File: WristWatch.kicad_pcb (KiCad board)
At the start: 4 copper layers, 59.9 x 59.9 mm, 144 parts

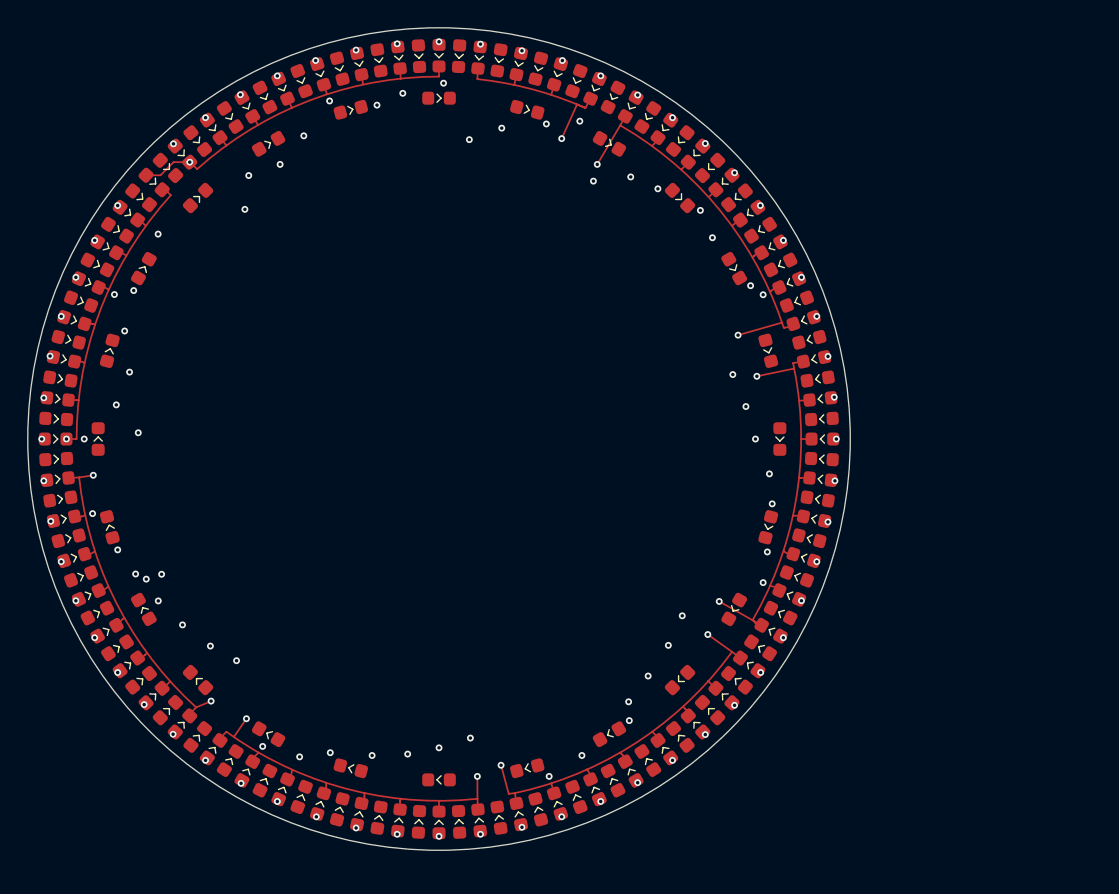
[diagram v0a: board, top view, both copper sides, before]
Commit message: Unknown progress. Pending twisted charlieplex experiments
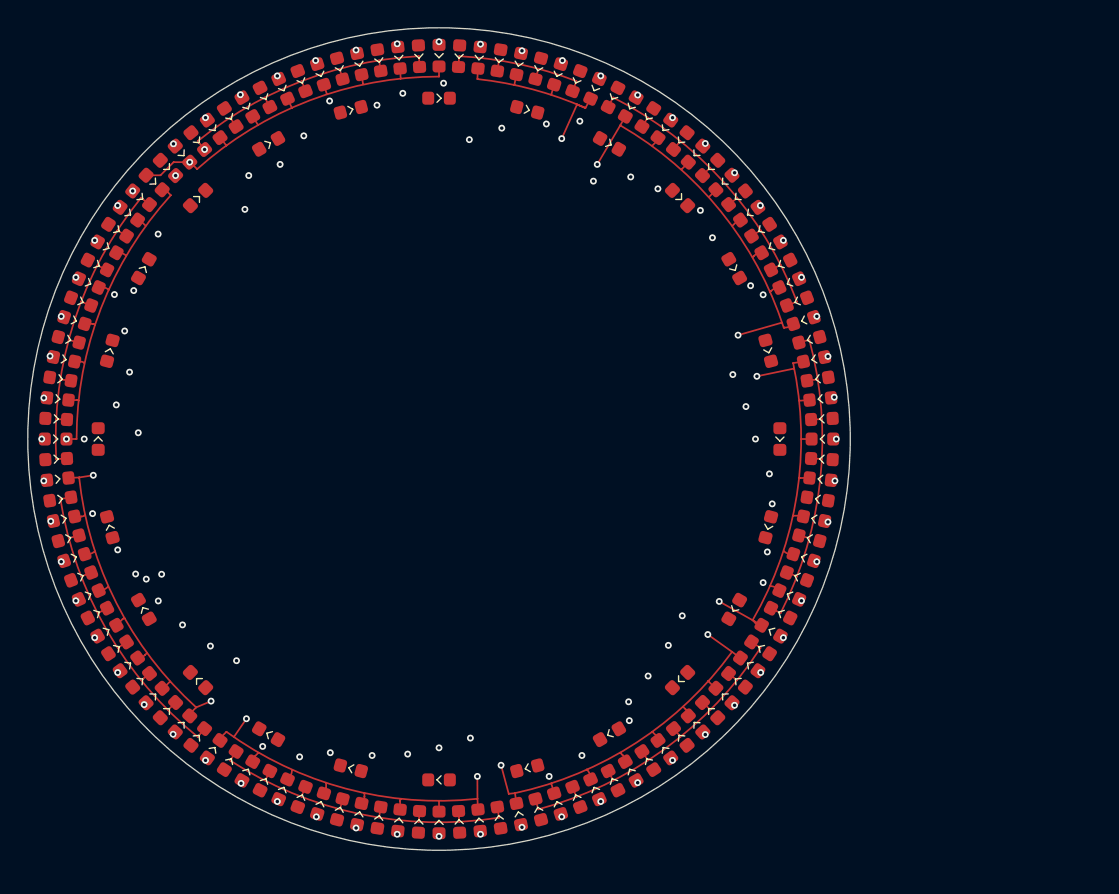
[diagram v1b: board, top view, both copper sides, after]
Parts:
- removed the D121 at (-6.43, -24.0)
- added D144: LED_Small, LED_SMD:LED_0603_1608Metric, F.Cu at (6.43, -24.0)
- D100, D101, D102, D103, D104, D105, D106, D107, D108, D109, D110, D111, D112, D113, D114, D115, D116, D117, D118, D119, D120, D61, D62, D63, D64, D65, D66, D67, D68, D69, D70, D71, D72, D73, D74, D75, D76, D77, D78, D79, D80, D81, D82, D83, D84, D85, D86, D87, D88, D89, D90, D91, D92, D93, D94, D95, D96, D97, D98, D99: value LED_0603_1608Metric -> LED_Small
- moved D126 6.48 mm to (-24.0, -6.43), turned to -105 degrees
- moved D127 6.48 mm to (-24.8, 0.00), turned to -90 degrees
- moved D132 6.48 mm to (-6.43, 24.0), turned to -15 degrees
- moved D133 6.48 mm to (0.00, 24.8), turned to 0 degrees
- moved D138 6.48 mm to (24.0, 6.43), turned to 75 degrees
- moved D139 6.48 mm to (24.8, 0.00), turned to 90 degrees
- moved D122 6.48 mm to (-6.43, -24.0), turned to -165 degrees
- moved D125 6.48 mm to (-21.5, -12.4), turned to -120 degrees
- moved D128 6.48 mm to (-24.0, 6.43), turned to -75 degrees
- moved D131 6.48 mm to (-12.4, 21.5), turned to -30 degrees
- moved D134 6.48 mm to (6.43, 24.0), turned to 15 degrees
- moved D137 6.48 mm to (21.5, 12.4), turned to 60 degrees
- moved D140 6.48 mm to (24.0, -6.43), turned to 105 degrees
- moved D143 6.48 mm to (12.4, -21.5), turned to 150 degrees
- moved D123 6.48 mm to (-12.4, -21.5), turned to -150 degrees
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- renumbered D1 to D121
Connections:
- D100 pad 1: (no net) -> CB5
- D100 pad 2: (no net) -> CB9
- D101 pad 1: (no net) -> CB6
- D101 pad 2: (no net) -> CB1
- D102 pad 1: (no net) -> CB6
- D102 pad 2: (no net) -> CB2
- D103 pad 1: (no net) -> CB6
- D103 pad 2: (no net) -> CB3
- D104 pad 1: (no net) -> CB6
- D104 pad 2: (no net) -> CB4
- D105 pad 1: (no net) -> CB6
- D105 pad 2: (no net) -> CB5
- D106 pad 1: (no net) -> CB6
- D106 pad 2: (no net) -> CB7
- D107 pad 1: (no net) -> CB6
- D107 pad 2: (no net) -> CB8
- D108 pad 1: (no net) -> CB6
- D108 pad 2: (no net) -> CB9
- D109 pad 1: (no net) -> CB7
- D109 pad 2: (no net) -> CB1
- D110 pad 1: (no net) -> CB7
- D110 pad 2: (no net) -> CB2
- D111 pad 1: (no net) -> CB7
- D111 pad 2: (no net) -> CB3
- D112 pad 1: (no net) -> CB7
- D112 pad 2: (no net) -> CB4
- D113 pad 1: (no net) -> CB7
- D113 pad 2: (no net) -> CB5
- D114 pad 1: (no net) -> CB7
- D114 pad 2: (no net) -> CB6
- D115 pad 1: (no net) -> CB7
- D115 pad 2: (no net) -> CB8
- D116 pad 1: (no net) -> CB7
- D116 pad 2: (no net) -> CB9
- D117 pad 1: (no net) -> CB8
- D117 pad 2: (no net) -> CB5
- D118 pad 1: (no net) -> CB8
- D118 pad 2: (no net) -> CB6
- D119 pad 1: (no net) -> CB8
- D119 pad 2: (no net) -> CB7
- D120 pad 1: (no net) -> CB8
- D120 pad 2: (no net) -> CB9
- D121 pad 1: (no net) -> CC1
- D121 pad 2: (no net) -> CC2
- D122 pad 1: (no net) -> CC1
- D122 pad 2: (no net) -> CC3
- D123 pad 1: (no net) -> CC1
- D123 pad 2: (no net) -> CC4
- D124 pad 1: (no net) -> CC1
- D124 pad 2: (no net) -> CC5
- D125 pad 1: (no net) -> CC1
- D125 pad 2: (no net) -> CC6
- D126 pad 1: (no net) -> CC2
- D126 pad 2: (no net) -> CC1
- D127 pad 1: (no net) -> CC2
- D127 pad 2: (no net) -> CC3
- D128 pad 1: (no net) -> CC2
- D128 pad 2: (no net) -> CC4
- D129 pad 1: (no net) -> CC2
- D129 pad 2: (no net) -> CC5
- D130 pad 1: (no net) -> CC2
- D130 pad 2: (no net) -> CC6
- D131 pad 1: (no net) -> CC3
- D131 pad 2: (no net) -> CC1
- D132 pad 1: (no net) -> CC3
- D132 pad 2: (no net) -> CC2
- D133 pad 1: (no net) -> CC3
- D133 pad 2: (no net) -> CC4
- D134 pad 1: (no net) -> CC3
- D134 pad 2: (no net) -> CC5
- D135 pad 1: (no net) -> CC3
- D135 pad 2: (no net) -> CC6
- D136 pad 1: (no net) -> CC4
- D136 pad 2: (no net) -> CC1
- D137 pad 1: (no net) -> CC4
- D137 pad 2: (no net) -> CC2
- D138 pad 1: (no net) -> CC4
- D138 pad 2: (no net) -> CC3
- D139 pad 1: (no net) -> CC4
- D139 pad 2: (no net) -> CC5
- D140 pad 1: (no net) -> CC4
- D140 pad 2: (no net) -> CC6
- D141 pad 1: (no net) -> CC5
- D141 pad 2: (no net) -> CC1
- D142 pad 1: (no net) -> CC5
- D142 pad 2: (no net) -> CC2
- D143 pad 1: (no net) -> CC5
- D143 pad 2: (no net) -> CC3
- D61 pad 1: (no net) -> CB1
- D61 pad 2: (no net) -> CB2
- D62 pad 1: (no net) -> CB1
- D62 pad 2: (no net) -> CB3
- D63 pad 1: (no net) -> CB1
- D63 pad 2: (no net) -> CB4
- D64 pad 1: (no net) -> CB1
- D64 pad 2: (no net) -> CB5
- D65 pad 1: (no net) -> CB1
- D65 pad 2: (no net) -> CB6
- D66 pad 1: (no net) -> CB1
- D66 pad 2: (no net) -> CB7
- D67 pad 1: (no net) -> CB1
- D67 pad 2: (no net) -> CB8
- D68 pad 1: (no net) -> CB1
- D68 pad 2: (no net) -> CB9
- D69 pad 1: (no net) -> CB2
- D69 pad 2: (no net) -> CB1
- D70 pad 1: (no net) -> CB2
- D70 pad 2: (no net) -> CB3
- D71 pad 1: (no net) -> CB2
- D71 pad 2: (no net) -> CB4
- D72 pad 1: (no net) -> CB2
- D72 pad 2: (no net) -> CB5
- D73 pad 1: (no net) -> CB2
- D73 pad 2: (no net) -> CB6
- D74 pad 1: (no net) -> CB2
- D74 pad 2: (no net) -> CB7
- D75 pad 1: (no net) -> CB2
- D75 pad 2: (no net) -> CB8
- D76 pad 1: (no net) -> CB2
- D76 pad 2: (no net) -> CB9
- D77 pad 1: (no net) -> CB3
- D77 pad 2: (no net) -> CB1
- D78 pad 1: (no net) -> CB3
- D78 pad 2: (no net) -> CB2
- D79 pad 1: (no net) -> CB3
- D79 pad 2: (no net) -> CB4
- D80 pad 1: (no net) -> CB3
- D80 pad 2: (no net) -> CB5
- D81 pad 1: (no net) -> CB3
- D81 pad 2: (no net) -> CB6
- D82 pad 1: (no net) -> CB3
- D82 pad 2: (no net) -> CB7
- D83 pad 1: (no net) -> CB3
- D83 pad 2: (no net) -> CB8
- D84 pad 1: (no net) -> CB3
- D84 pad 2: (no net) -> CB9
- D85 pad 1: (no net) -> CB4
- D85 pad 2: (no net) -> CB1
- D86 pad 1: (no net) -> CB4
- D86 pad 2: (no net) -> CB2
- D87 pad 1: (no net) -> CB4
- D87 pad 2: (no net) -> CB3
- D88 pad 1: (no net) -> CB4
- D88 pad 2: (no net) -> CB5
- D89 pad 1: (no net) -> CB4
- D89 pad 2: (no net) -> CB6
- D90 pad 1: (no net) -> CB4
- D90 pad 2: (no net) -> CB7
- D91 pad 1: (no net) -> CB4
- D91 pad 2: (no net) -> CB8
- D92 pad 1: (no net) -> CB4
- D92 pad 2: (no net) -> CB9
- D93 pad 1: (no net) -> CB5
- D93 pad 2: (no net) -> CB1
- D94 pad 1: (no net) -> CB5
- D94 pad 2: (no net) -> CB2
- D95 pad 1: (no net) -> CB5
- D95 pad 2: (no net) -> CB3
- D96 pad 1: (no net) -> CB5
- D96 pad 2: (no net) -> CB4
- D97 pad 1: (no net) -> CB5
- D97 pad 2: (no net) -> CB6
- D98 pad 1: (no net) -> CB5
- D98 pad 2: (no net) -> CB7
- D99 pad 1: (no net) -> CB5
- D99 pad 2: (no net) -> CB8
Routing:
- net CB5: track 0.00 -> 6.31 mm
- net CB7: track 0.00 -> 6.27 mm
- net CB2: track 0.00 -> 6.24 mm
- net CB4: track 0.00 -> 6.23 mm
- net CB3: track 0.00 -> 6.16 mm
- net CB1: track 0.00 -> 5.51 mm, vias 0 -> 3
- net CB6: track 0.00 -> 5.45 mm
- net CB8: track 0.00 -> 3.13 mm

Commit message: Start layout. MCU close, LEDs correct, pending esp32
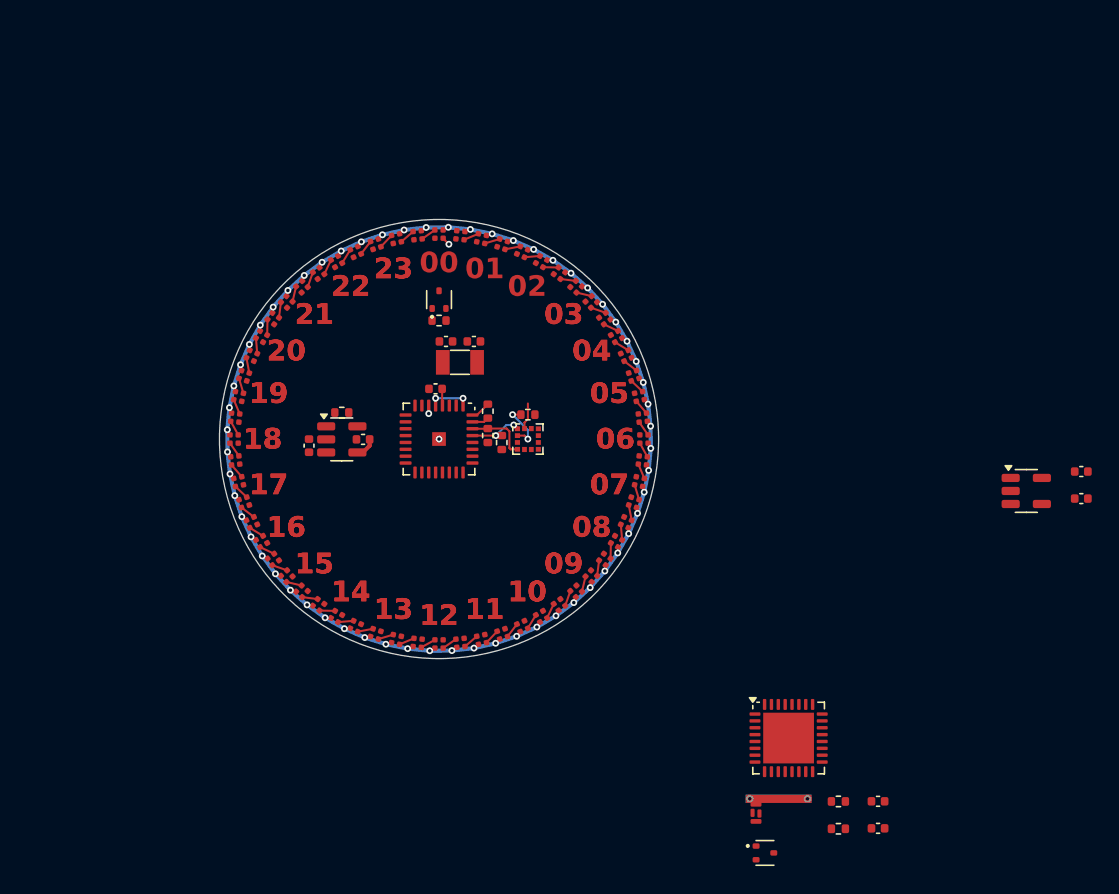
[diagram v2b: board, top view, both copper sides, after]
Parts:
- removed D100, D101, D102, D103, D104, D105, D106, D107, D108, D109, D110, D111, D112, D113, D114, D115, D116, D117, D118, D119, D120, D121, D122, D123, D124, D125, D126, D127, D128, D129, D130, D131, D132, D133, D134, D135, D136, D137, D138, D139, D140, D141, D142, D143, D144, D61, D62, D63, D64, D65, D66, D67, D68, D69, D70, D71, D72, D73, D74, D75, D76, D77, D78, D79, D80, D81, D82, D83, D84, D85, D86, D87, D88, D89, D90, D91, D92, D93, D94, D95, D96, D97, D98, D99: LED_Small, LED_SMD:LED_0603_1608Metric
- added AE1: Antenna_Shield, Antenna_SMD:C209892, F.Cu at (23.1, 27.8)
- added C1: 100n, Capacitor_SMD:C_0402_1005Metric, F.Cu at (-0.25, -3.66)
- added C12: 1u, Capacitor_SMD:C_0402_1005Metric, F.Cu at (46.8, 2.37)
- added C13: 2u2, Capacitor_SMD:C_0402_1005Metric, F.Cu at (46.8, 4.34)
- added C14: 4u7, Capacitor_SMD:C_0402_1005Metric, F.Cu at (-5.54, 0.03)
- added C15: 4u7, Capacitor_SMD:C_0402_1005Metric, F.Cu at (-9.47, 0.48)
- added C16: 12p, Capacitor_SMD:C_0402_1005Metric, F.Cu at (32.0, 26.4)
- added C17: 12p, Capacitor_SMD:C_0402_1005Metric, F.Cu at (32.0, 28.4)
- added C4: 4p3, Capacitor_SMD:C_0402_1005Metric, F.Cu at (2.54, -7.11)
- added C7: 4p3, Capacitor_SMD:C_0402_1005Metric, F.Cu at (0.51, -7.11)
- added Q1: Q_PMOS_GSD, Package_TO_SOT_SMD:SOT-523, F.Cu at (0.00, -10.2)
- added Q2: Q_PMOS_GSD, Package_TO_SOT_SMD:SOT-523, F.Cu at (23.8, 30.2)
- added R1: 10k, Resistor_SMD:R_0402_1005Metric, F.Cu at (3.56, -2.03)
- added R10: 10k, Resistor_SMD:R_0402_1005Metric, F.Cu at (-7.09, -1.93)
- added R11: 1M, Resistor_SMD:R_0402_1005Metric, F.Cu at (29.1, 26.4)
- added R12: 100k, Resistor_SMD:R_0402_1005Metric, F.Cu at (29.1, 28.4)
- added R6: 1M, Resistor_SMD:R_0402_1005Metric, F.Cu at (0.00, -8.64)
- added R7: 4k7, Resistor_SMD:R_0402_1005Metric, F.Cu at (4.57, 0.25)
- added R8: 4k7, Resistor_SMD:R_0402_1005Metric, F.Cu at (3.56, -0.25)
- added R9: 10k, Resistor_SMD:R_0402_1005Metric, F.Cu at (6.48, -1.78)
- added U2: STM32L412KBUx, Package_DFN_QFN:QFN-32-1EP_5x5mm_P0.5mm_EP3.45x3.45mm, F.Cu at (0.00, 0.00)
- added U3: LIS2DE12, Package_LGA:LGA-12_2x2mm_P0.5mm, F.Cu at (6.48, 0.00)
- added U4: AP2205-3.0, Package_TO_SOT_SMD:SOT-23-5, F.Cu at (42.8, 3.78)
- added U5: MCP73832-2-OT, Package_TO_SOT_SMD:SOT-23-5, F.Cu at (-7.09, 0.03)
- added U6: ESP32-C3, Package_DFN_QFN:QFN-32-1EP_5x5mm_P0.5mm_EP3.7x3.7mm, F.Cu at (25.5, 21.8)
- added Y1: 32.768k, Crystal:Crystal_SMD_3215-2Pin_3.2x1.5mm, F.Cu at (1.52, -5.59)
- D1, D10, D11, D12, D13, D14, D15, D16, D17, D18, D19, D2, D20, D21, D22, D23, D24, D25, D26, D27, D28, D29, D3, D30, D31, D32, D33, D34, D35, D36, D37, D38, D39, D4, D40, D41, D42, D43, D44, D45, D46, D47, D48, D49, D5, D50, D51, D52, D53, D54, D55, D56, D57, D58, D59, D6, D60, D7, D8, D9: value LED_Small -> WS2812B; footprint LED_SMD:LED_0603_1608Metric -> LED_Custom:XL-1010RGBC
- moved D15 13.0 mm to (-14.9, -1.56), turned to 84 degrees
- moved D17 13.0 mm to (-14.9, 1.56), turned to 96 degrees
- moved D2 13.0 mm to (-1.56, -14.9), turned to 6 degrees
- moved D30 13.0 mm to (-1.56, 14.9), turned to 174 degrees
- moved D32 13.0 mm to (1.56, 14.9), turned to -174 degrees
- moved D45 13.0 mm to (14.9, 1.56), turned to -96 degrees
- moved D47 13.0 mm to (14.9, -1.56), turned to -84 degrees
- moved D60 13.0 mm to (1.56, -14.9), turned to -6 degrees
- moved D12 13.0 mm to (-13.6, -6.07), turned to 66 degrees
- moved D20 13.0 mm to (-13.6, 6.07), turned to 114 degrees
- moved D27 13.0 mm to (-6.07, 13.6), turned to 156 degrees
- moved D35 13.0 mm to (6.07, 13.6), turned to -156 degrees
- moved D42 13.0 mm to (13.6, 6.07), turned to -114 degrees
- moved D5 13.0 mm to (-6.07, -13.6), turned to 24 degrees
- moved D50 13.0 mm to (13.6, -6.07), turned to -66 degrees
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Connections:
- D1 pad 1: CA1 -> VLED
- D1 pad 2: CA2 -> Net-(D1-DOUT)
- D10 pad 1: CA2 -> VLED
- D10 pad 2: CA3 -> Net-(D10-DOUT)
- D11 pad 1: CA2 -> VLED
- D11 pad 2: CA4 -> Net-(D11-DOUT)
- D12 pad 1: CA2 -> VLED
- D12 pad 2: CA5 -> Net-(D12-DOUT)
- D13 pad 1: CA2 -> VLED
- D13 pad 2: CA6 -> Net-(D13-DOUT)
- D14 pad 1: CA2 -> VLED
- D14 pad 2: CA7 -> Net-(D14-DOUT)
- D15 pad 1: CA2 -> VLED
- D15 pad 2: CA8 -> Bank1
- D16 pad 1: CA2 -> VLED
- D16 pad 2: CA9 -> Net-(D16-DOUT)
- D17 pad 1: CA3 -> VLED
- D17 pad 2: CA1 -> Net-(D17-DOUT)
- D18 pad 1: CA3 -> VLED
- D18 pad 2: CA2 -> Net-(D18-DOUT)
- D19 pad 1: CA3 -> VLED
- D19 pad 2: CA4 -> Net-(D19-DOUT)
- D2 pad 1: CA1 -> VLED
- D2 pad 2: CA3 -> Net-(D2-DOUT)
- D20 pad 1: CA3 -> VLED
- D20 pad 2: CA5 -> Net-(D20-DOUT)
- D21 pad 1: CA3 -> VLED
- D21 pad 2: CA6 -> Net-(D21-DOUT)
- D22 pad 1: CA3 -> VLED
- D22 pad 2: CA7 -> Net-(D22-DOUT)
- D23 pad 1: CA3 -> VLED
- D23 pad 2: CA8 -> Net-(D23-DOUT)
- D24 pad 1: CA3 -> VLED
- D24 pad 2: CA9 -> Net-(D24-DOUT)
- D25 pad 1: CA4 -> VLED
- D25 pad 2: CA1 -> Net-(D25-DOUT)
- D26 pad 1: CA4 -> VLED
- D26 pad 2: CA2 -> Net-(D26-DOUT)
- D27 pad 1: CA4 -> VLED
- D27 pad 2: CA3 -> Net-(D27-DOUT)
- D28 pad 1: CA4 -> VLED
- D28 pad 2: CA5 -> Net-(D28-DOUT)
- D29 pad 1: CA4 -> VLED
- D29 pad 2: CA6 -> Net-(D29-DOUT)
- D3 pad 1: CA1 -> VLED
- D3 pad 2: CA4 -> Net-(D3-DOUT)
- D30 pad 1: CA4 -> VLED
- D30 pad 2: CA7 -> Bank2
- D31 pad 1: CA4 -> VLED
- D31 pad 2: CA8 -> Net-(D31-DOUT)
- D32 pad 1: CA4 -> VLED
- D32 pad 2: CA9 -> Net-(D32-DOUT)
- D33 pad 1: CA5 -> VLED
- D33 pad 2: CA1 -> Net-(D33-DOUT)
- D34 pad 1: CA5 -> VLED
- D34 pad 2: CA2 -> Net-(D34-DOUT)
- D35 pad 1: CA5 -> VLED
- D35 pad 2: CA3 -> Net-(D35-DOUT)
- D36 pad 1: CA5 -> VLED
- D36 pad 2: CA4 -> Net-(D36-DOUT)
- D37 pad 1: CA5 -> VLED
- D37 pad 2: CA6 -> Net-(D37-DOUT)
- D38 pad 1: CA5 -> VLED
- D38 pad 2: CA7 -> Net-(D38-DOUT)
- D39 pad 1: CA5 -> VLED
- D39 pad 2: CA8 -> Net-(D39-DOUT)
- D4 pad 1: CA1 -> VLED
- D4 pad 2: CA5 -> Net-(D4-DOUT)
- D40 pad 1: CA5 -> VLED
- D40 pad 2: CA9 -> Net-(D40-DOUT)
- D41 pad 1: CA6 -> VLED
- D41 pad 2: CA1 -> Net-(D41-DOUT)
- D42 pad 1: CA6 -> VLED
- D42 pad 2: CA2 -> Net-(D42-DOUT)
- D43 pad 1: CA6 -> VLED
- D43 pad 2: CA3 -> Net-(D43-DOUT)
- D44 pad 1: CA6 -> VLED
- D44 pad 2: CA4 -> Net-(D44-DOUT)
- D45 pad 1: CA6 -> VLED
- D45 pad 2: CA5 -> Bank3
- D46 pad 1: CA6 -> VLED
- D46 pad 2: CA7 -> Net-(D46-DOUT)
- D47 pad 1: CA6 -> VLED
- D47 pad 2: CA8 -> Net-(D47-DOUT)
- D48 pad 1: CA6 -> VLED
- D48 pad 2: CA9 -> Net-(D48-DOUT)
- D49 pad 1: CA7 -> VLED
- D49 pad 2: CA1 -> Net-(D49-DOUT)
- D5 pad 1: CA1 -> VLED
- D5 pad 2: CA6 -> Net-(D5-DOUT)
- D50 pad 1: CA7 -> VLED
- D50 pad 2: CA2 -> Net-(D50-DOUT)
- D51 pad 1: CA7 -> VLED
- D51 pad 2: CA3 -> Net-(D51-DOUT)
- D52 pad 1: CA7 -> VLED
- D52 pad 2: CA4 -> Net-(D52-DOUT)
- D53 pad 1: CA7 -> VLED
- D53 pad 2: CA5 -> Net-(D53-DOUT)
- D54 pad 1: CA7 -> VLED
- D54 pad 2: CA6 -> Net-(D54-DOUT)
- D55 pad 1: CA7 -> VLED
- D55 pad 2: CA8 -> Net-(D55-DOUT)
- D56 pad 1: CA7 -> VLED
- D56 pad 2: CA9 -> Net-(D56-DOUT)
- D57 pad 1: CA8 -> VLED
- D57 pad 2: CA5 -> Net-(D57-DOUT)
- D58 pad 1: CA8 -> VLED
- D58 pad 2: CA6 -> Net-(D58-DOUT)
- D59 pad 1: CA8 -> VLED
- D59 pad 2: CA7 -> Net-(D59-DOUT)
- D6 pad 1: CA1 -> VLED
- D6 pad 2: CA7 -> Net-(D6-DOUT)
- D60 pad 1: CA8 -> VLED
- D60 pad 2: CA9 -> unconnected-(D60-DOUT-Pad2)
- D7 pad 1: CA1 -> VLED
- D7 pad 2: CA8 -> Net-(D7-DOUT)
- D8 pad 1: CA1 -> VLED
- D8 pad 2: CA9 -> Net-(D8-DOUT)
- D9 pad 1: CA2 -> VLED
- D9 pad 2: CA1 -> Net-(D10-DIN)
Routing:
- net VLED: track 0.00 -> 122.5 mm, vias 0 -> 60
- net CA9: track 56.8 -> 0.00 mm, vias 16 -> 0
- net CA7: track 53.8 -> 0.00 mm, vias 16 -> 0
- net CA8: track 49.4 -> 0.00 mm, vias 17 -> 0
- net CA6: track 48.1 -> 0.00 mm, vias 16 -> 0
- net CA5: track 40.5 -> 0.00 mm, vias 16 -> 0
- net CA4: track 38.2 -> 0.00 mm, vias 14 -> 0
- net CA3: track 30.9 -> 0.00 mm, vias 14 -> 0
- net CA2: track 25.9 -> 0.00 mm, vias 14 -> 0
- net CA1: track 21.5 -> 0.00 mm, vias 6 -> 0
- net CB5: track 6.31 -> 0.00 mm
- net CB7: track 6.27 -> 0.00 mm
- net CB2: track 6.24 -> 0.00 mm
- net CB4: track 6.23 -> 0.00 mm
- net CB3: track 6.16 -> 0.00 mm
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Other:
- board size 59.9 x 59.9 mm -> 32 x 32 mm
- board text added: "00"
- board text added: "01"
- board text added: "02"
- board text added: "03"
- board text added: "04"
- board text added: "05"
- board text added: "06"
- board text added: "07"
- board text added: "08"
- board text added: "09"
- board text added: "10"
- board text added: "11"
- board text added: "12"
- board text added: "13"
- board text added: "14"
- board text added: "15"
- board text added: "16"
- board text added: "17"
- board text added: "18"
- board text added: "19"
- board text added: "20"
- board text added: "21"
- board text added: "22"
- board text added: "23"
